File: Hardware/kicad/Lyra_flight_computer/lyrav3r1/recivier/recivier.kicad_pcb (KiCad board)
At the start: 2 copper layers, 74 parts, among them J1 USB_B_Micro, J2 Conn_01x02, J3 Conn_01x02, Q1 AO3401A, SW1 K2-1102DP-L3SW-04, SW2 K2-1102DP-L3SW-04, SW3 K2-1102DP-L3SW-04, SW4 K2-1102DP-L3SW-04, SW5 K2-1102DP-L3SW-04, U1 E22-900MM22S, U2 W25Q128JVS, U3 RP2040, U4 TXB0104RGY, U5 PCM5102A, U6 ATGM336H-5N31, U7 LIS3MDLTR, U8 RT9013-33GB_C19268157, U9 AMS1117-5.0, X1 SX1M12.000M10F30TNN

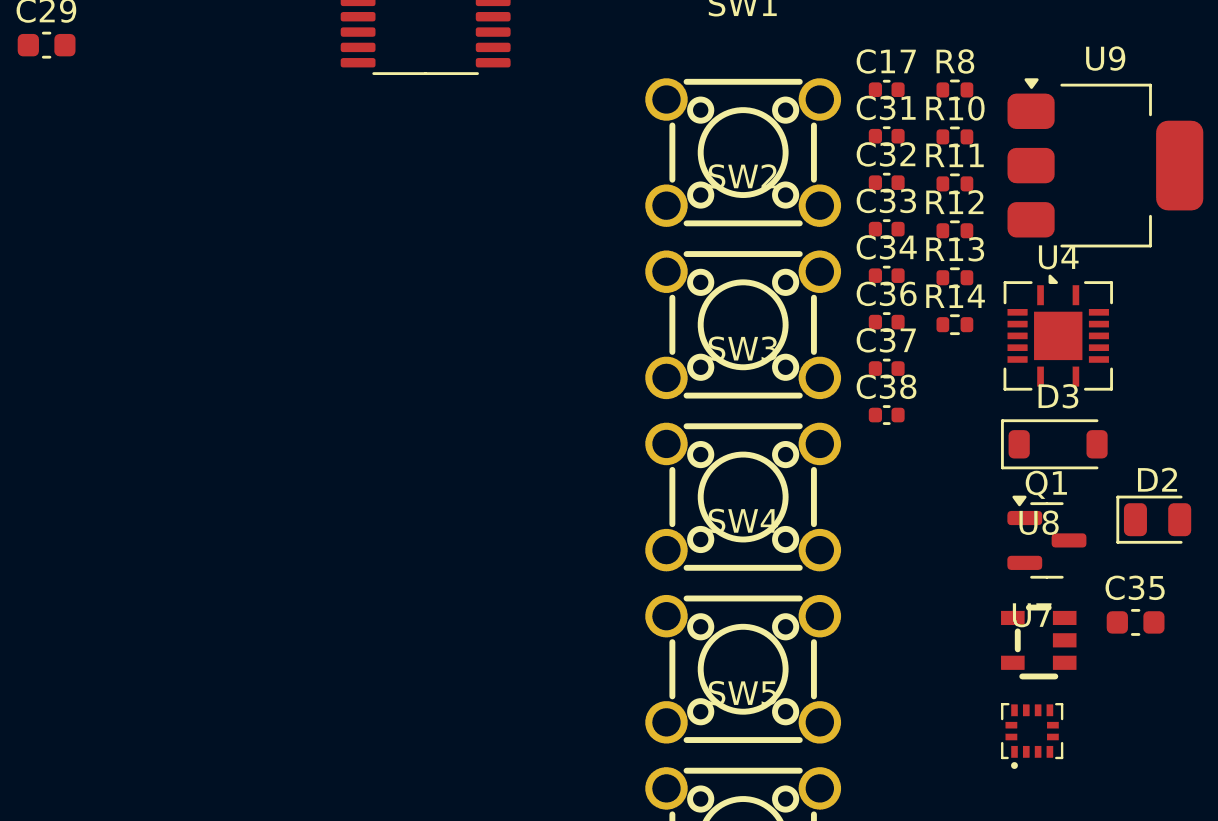
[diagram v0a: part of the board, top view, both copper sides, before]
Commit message: added batt protection for lyra, added more parts for reciver
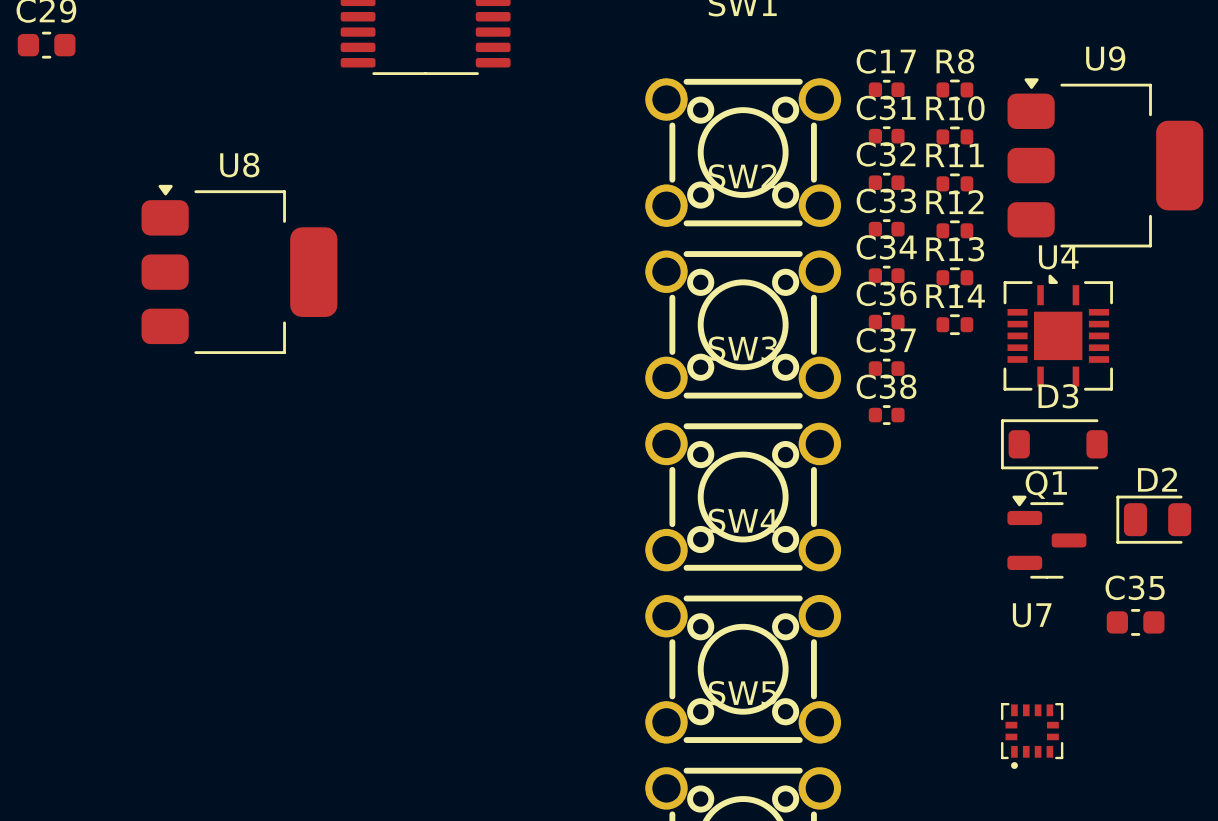
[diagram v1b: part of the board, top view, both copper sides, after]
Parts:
- U8: value RT9013-33GB_C19268157 -> AMS1117-3.3; footprint .pretty:SOT-23-5_L2.9-W1.6-P0.95-LS2.8-BR -> Package_TO_SOT_SMD:SOT-223-3_TabPin2
- moved U8 37.3 mm to (142.2, 107.9)
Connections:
- R10 pad 1: Net-(R10-Pad1) -> /BUTTON5
- R10 pad 2: /BUTTON3 -> GND
- R11 pad 1: Net-(R11-Pad1) -> /BUTTON2
- R11 pad 2: /BUTTON4 -> GND
- R12 pad 1: Net-(R10-Pad1) -> /BUTTON3
- R12 pad 2: /BUTTON1 -> GND
- R13 pad 1: Net-(R10-Pad1) -> /BUTTON1
- R13 pad 2: /BUTTON5 -> GND
- R8 pad 1: +3.3VA -> /BUTTON4
- R8 pad 2: /BUTTON2 -> GND
- SW1 pad 1: Net-(R10-Pad1) -> Net-(SW1-Pad1)
- SW1 pad 2: Net-(R11-Pad1) -> Net-(SW1-Pad2)
- SW2 pad 2: Net-(R10-Pad1) -> Net-(SW1-Pad1)
- SW3 pad 1: Net-(R10-Pad1) -> Net-(SW1-Pad1)
- SW3 pad 2: Net-(R11-Pad1) -> Net-(SW1-Pad2)
- SW4 pad 1: Net-(R11-Pad1) -> Net-(SW1-Pad2)
- SW4 pad 2: Net-(R11-Pad1) -> Net-(SW1-Pad2)
- SW5 pad 1: Net-(R10-Pad1) -> Net-(SW1-Pad1)
- SW5 pad 2: Net-(R11-Pad1) -> Net-(SW1-Pad2)
- U3 pad 30: unconnected-(U3-GPIO19-Pad30) -> /BUTTON1
- U3 pad 31: unconnected-(U3-GPIO20-Pad31) -> /BUTTON2
- U3 pad 32: unconnected-(U3-GPIO21-Pad32) -> /BUTTON3
- U3 pad 34: unconnected-(U3-GPIO22-Pad34) -> /BUTTON4
- U3 pad 35: unconnected-(U3-GPIO23-Pad35) -> /BUTTON5
- U8 pad 1: +BATT -> GND
- U8 pad 2: GND -> +3.3VA

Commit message: reciver work and finalized lyrav3r1
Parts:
- added C20: 2u2, Capacitor_SMD:C_0603_1608Metric, F.Cu at (195.6, 120.3)
- added C21: 2u2, Capacitor_SMD:C_0603_1608Metric, F.Cu at (200.9, 116.2)
- added C30: 2u2, Capacitor_SMD:C_0603_1608Metric, F.Cu at (204.6, 112.4)
- added D1: LED, LED_SMD:LED_0805_2012Metric, F.Cu at (199.1, 53.3)
- added J4: Screw_Terminal_01x02, TerminalBlock:TerminalBlock_bornier-2_P5.08mm, F.Cu at (204.2, 108.9)
- added J5: Screw_Terminal_01x02, TerminalBlock:TerminalBlock_bornier-2_P5.08mm, F.Cu at (143.2, 112.4)
- added R16: 1k, Resistor_SMD:R_0402_1005Metric, F.Cu at (154.5, 122.5)
- added R17: 40k, Resistor_SMD:R_0402_1005Metric, F.Cu at (153.5, 122.5)
- added R7: 1k, Resistor_SMD:R_0402_1005Metric, F.Cu at (201.8, 53.4)
- added R9: 470, Resistor_SMD:R_0402_1005Metric, F.Cu at (203.8, 114.1)
- added RV1: R_Potentiometer, .pretty:RES-ADJ-SMD_3314J, F.Cu at (186.9, 102.1)
- added SW6: SW_SPDT, .pretty:SW-TH_SK12D07VG4, F.Cu at (141.6, 104.5)
- DS1: footprint Display:AG12864E -> .pretty:ST7920 AZ
- J2, TP1: moved to B.Cu
- moved DS1 106.9 mm to (141.6, 97.1), turned to 90 degrees
- moved H4 99.2 mm to (205.7, 124.2)
- moved H2 90.0 mm to (205.7, 50.2)
- moved AE2 84.3 mm to (197.9, 72.1)
- moved U6 75.8 mm to (201.1, 64.7)
- moved C26 70.9 mm to (199.9, 118.2), turned to 90 degrees
- moved C27 70.7 mm to (201.1, 118.4), turned to 90 degrees
- moved C25 70.0 mm to (201.1, 113.4), turned to 90 degrees
- moved C24 69.7 mm to (199.9, 113.8), turned to 90 degrees
- moved AE1 67.5 mm to (173.6, 50.0)
- moved C23 63.6 mm to (189.7, 116.2), turned to 90 degrees
- moved C28 62.7 mm to (191.2, 118.5), turned to 90 degrees
- moved C22 62.3 mm to (191.0, 116.1), turned to 90 degrees
- moved C29 59.0 mm to (189.5, 118.6), turned to 90 degrees
- moved H3 57.2 mm to (141.7, 124.2)
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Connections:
- C35 pad 1: +BATT -> Net-(Q1-S)
- Card1 pad 5: /SCK -> /SCLK
- DS1 pad 4: /LCD CS -> /LCD CS 5V
- DS1 pad 6: /SCK 2 5V -> /SCLK 2 5V
- Q1 pad 2: +BATT -> Net-(Q1-S)
- SW1 pad 1: Net-(SW1-Pad1) -> +3.3VA
- SW1 pad 2: Net-(SW1-Pad2) -> unconnected-(SW1-Pad2)
- SW1 pad 4: /BUTTON1 -> unconnected-(SW1-Pad4)
- SW2 pad 1: +3.3VA -> unconnected-(SW2-Pad1)
- SW2 pad 2: Net-(SW1-Pad1) -> +3.3VA
- SW2 pad 4: /BUTTON2 -> unconnected-(SW2-Pad4)
- SW3 pad 1: Net-(SW1-Pad1) -> +3.3VA
- SW3 pad 2: Net-(SW1-Pad2) -> unconnected-(SW3-Pad2)
- SW3 pad 4: /BUTTON3 -> unconnected-(SW3-Pad4)
- SW4 pad 1: Net-(SW1-Pad2) -> +3.3VA
- SW4 pad 2: Net-(SW1-Pad2) -> unconnected-(SW4-Pad2)
- SW4 pad 4: /BUTTON4 -> unconnected-(SW4-Pad4)
- SW5 pad 1: Net-(SW1-Pad1) -> +3.3VA
- SW5 pad 2: Net-(SW1-Pad2) -> unconnected-(SW5-Pad2)
- SW5 pad 4: /BUTTON5 -> unconnected-(SW5-Pad4)
- U1 pad 15: /SCK -> /SCLK
- U3 pad 11: /LCD CS -> /BCK
- U3 pad 12: /SD_CS -> /SCK
- U3 pad 13: unconnected-(U3-GPIO10-Pad13) -> /DIN
- U3 pad 14: unconnected-(U3-GPIO11-Pad14) -> /LRCK
- U3 pad 17: unconnected-(U3-GPIO14-Pad17) -> /LCD CS
- U3 pad 18: /LRCK -> unconnected-(U3-GPIO15-Pad18)
- U3 pad 2: /RXEN -> /BUTTON2
- U3 pad 27: /DIN -> unconnected-(U3-GPIO16-Pad27)
- U3 pad 28: /BCK -> unconnected-(U3-GPIO17-Pad28)
- U3 pad 29: /SCK -> unconnected-(U3-GPIO18-Pad29)
- U3 pad 3: /TXEN -> /BUTTON5
- U3 pad 30: /BUTTON1 -> /SX RST
- U3 pad 31: /BUTTON2 -> /BUSY
- U3 pad 32: /BUTTON3 -> /SX CS
- U3 pad 34: /BUTTON4 -> /SCLK
- U3 pad 35: /BUTTON5 -> /MOSI
- U3 pad 36: unconnected-(U3-GPIO24-Pad36) -> /MISO
- U3 pad 38: unconnected-(U3-GPIO26_ADC0-Pad38) -> /SD_CS
- U3 pad 39: unconnected-(U3-GPIO27_ADC1-Pad39) -> /TXEN
- U3 pad 4: /SX RST -> /BUTTON3
- U3 pad 40: unconnected-(U3-GPIO28_ADC2-Pad40) -> /RXEN
- U3 pad 41: unconnected-(U3-GPIO29_ADC3-Pad41) -> /BATT SENSE
- U3 pad 5: /MOSI -> /BUTTON4
- U3 pad 6: /MISO -> /BUTTON1
- U3 pad 7: /SX CS -> unconnected-(U3-GPIO5-Pad7)
- U3 pad 8: /SCK -> unconnected-(U3-GPIO6-Pad8)
- U3 pad 9: /BUSY -> unconnected-(U3-GPIO7-Pad9)
- U4 pad 11: /MOSI 2 5V -> /SCLK 2 5V
- U4 pad 12: /LCD CS -> /MOSI 2 5V
- U4 pad 13: /SCK 2 5V -> /LCD CS 5V
- U4 pad 2: /SCK -> /LCD CS
- U4 pad 3: /LCD CS -> /MOSI
- U4 pad 4: /MOSI -> /SCLK
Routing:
- net GND: track 0.00 -> 85.5 mm, vias 0 -> 54
- net /SCL: track 0.00 -> 65.8 mm
- net /MOSI: track 0.00 -> 64.9 mm, vias 0 -> 4
- net VBUS: track 0.00 -> 64.7 mm, vias 0 -> 2
- net /LRCK: track 0.00 -> 62.4 mm
- net +5V: track 0.00 -> 62.3 mm, vias 0 -> 2
- net /BATT SENSE: track 0.00 -> 61.2 mm, vias 0 -> 2
- net /SDA: track 0.00 -> 59.7 mm, vias 0 -> 2
- net /BCK: track 0.00 -> 57.8 mm
- net /DIN: track 0.00 -> 56.5 mm
- net /SCK: track 0.00 -> 55.7 mm
- net /SCLK: track 0.00 -> 55.5 mm, vias 0 -> 4
- net +3.3VA: track 0.00 -> 54.6 mm, vias 0 -> 27
- net /BUTTON3: track 0.00 -> 54.1 mm
- net /BUTTON5: track 0.00 -> 52.8 mm
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- added copper zone on In2.Cu, net +3.3VA
- added copper zone on In1.Cu, net GND
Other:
- board outline added: 70 x 80 mm
- copper layers 2 -> 4

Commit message: work, lyra mostly final
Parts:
- added D4: LED, LED_SMD:LED_0805_2012Metric, F.Cu at (177.0, 77.1)
- added R15: 1k, Resistor_SMD:R_0402_1005Metric, F.Cu at (174.2, 77.3)
- moved R12 37.0 mm to (156.1, 90.4)
- moved R8 36.7 mm to (157.3, 88.7), turned to 180 degrees
- moved R10 36.7 mm to (154.3, 93.0), turned to 180 degrees
- moved R11 27.5 mm to (152.4, 91.3)
- moved R13 26.0 mm to (160.2, 90.3)
- moved AE2 1.24 mm to (197.9, 73.4)
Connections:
- U3 pad 18: unconnected-(U3-GPIO15-Pad18) -> /LEDINDICATION
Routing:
- net /LEDINDICATION: track 0.00 -> 14.9 mm
- net /BUTTON3: track 54.1 -> 43.5 mm
- net /LRCK: track 62.4 -> 58.4 mm
- net /SCL: track 65.8 -> 68.6 mm
- net /SDA: track 59.7 -> 61.8 mm
- net /BUTTON5: track 52.8 -> 50.8 mm
- net /BUTTON2: track 43.5 -> 41.9 mm
- net /BUTTON4: track 50.7 -> 49.2 mm
- net Net-(D4-K): track 0.00 -> 1.42 mm
- net /BCK: track 57.8 -> 56.5 mm
- net /ANT: track 1.90 -> 3.13 mm
- net +3.3VA: track 54.6 -> 55.3 mm, vias 27 -> 28
- net /SCK: track 55.7 -> 55.2 mm
- net GND: track 85.5 -> 85.6 mm, vias 54 -> 55

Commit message: reciver rework
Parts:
- removed DS1: ST7920, .pretty:ST7920 AZ

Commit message: stuffs
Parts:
- removed C31, C37, C38: 1u, Capacitor_SMD:C_0402_1005Metric
- removed Card1: TF-115K, .pretty:TF-SMD_TF-115K
- removed J4: Screw_Terminal_01x02, TerminalBlock:TerminalBlock_bornier-2_P5.08mm
- removed RV1: R_Potentiometer, .pretty:RES-ADJ-SMD_3314J
- removed SW1, SW2, SW3, SW4, SW5: K2-1102DP-L3SW-04, .pretty:SW-TH_4P-L6.0-W6.0-P4.50-LS6.5
- removed U4: TXB0104RGY, Package_DFN_QFN:Texas_S-PVQFN-N14
- removed U9: AMS1117-5.0, Package_TO_SOT_SMD:SOT-223-3_TabPin2
- added C16: 100n, Capacitor_SMD:C_0402_1005Metric, F.Cu at (180.9, 124.9)
- added C18: 10u, Capacitor_SMD:C_0603_1608Metric, F.Cu at (182.2, 125.5)
- added C19: 2u2, Capacitor_SMD:C_0603_1608Metric, F.Cu at (194.3, 137.6)
- added D5: ER-TFT032A3-3, .pretty:R-TFT032IPS-3.2, F.Cu at (146.5, 122.2)
- added J6: Conn_01x08, Connector_PinSocket_2.54mm:PinSocket_1x08_P2.54mm_Vertical, F.Cu at (153.8, 145.3)
- added J8: AudioJack4, .pretty:AUDIO-SMD_PJ-320D, F.Cu at (194.1, 128.6)
- added R18: 5.1k, Resistor_SMD:R_0402_1005Metric, F.Cu at (157.4, 129.9)
- added R19: 5.1k, Resistor_SMD:R_0402_1005Metric, F.Cu at (157.4, 127.6)
- added R20: 470, Resistor_SMD:R_0402_1005Metric, F.Cu at (192.1, 137.3)
- moved R13 52.4 mm to (157.6, 142.6)
- moved R11 49.2 mm to (157.6, 140.3), turned to 0 degrees
- moved R12 47.3 mm to (157.5, 137.7)
- moved R8 46.4 mm to (157.5, 135.1), turned to 0 degrees
- moved R10 39.7 mm to (157.4, 132.6), turned to 0 degrees
- moved C17 36.7 mm to (184.2, 91.6), turned to 180 degrees
- moved D2 30.4 mm to (173.8, 107.3), turned to -90 degrees
- moved D1 27.9 mm to (186.6, 78.2)
- moved R7 27.7 mm to (189.5, 78.3)
- moved R14 26.7 mm to (173.8, 110.0), turned to -90 degrees
- moved U6 25.5 mm to (191.4, 88.3), turned to 90 degrees
- moved C30 25.2 mm to (193.4, 135.0), turned to -90 degrees
- moved C27 24.8 mm to (188.7, 139.9)
- moved C26 24.8 mm to (187.5, 139.6)
- moved C21 24.8 mm to (188.5, 137.6)
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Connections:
- net /AUDIOOUT renamed /AUDIOOUT R
- U3 pad 11: /BCK -> /SCK
- U3 pad 12: /SCK -> /DIN
- U3 pad 13: /DIN -> /LRCK
- U3 pad 14: /LRCK -> /LCD RST
- U3 pad 18: /LEDINDICATION -> /LCD D/C
- U3 pad 2: /BUTTON2 -> /BUTTON7
- U3 pad 29: unconnected-(U3-GPIO18-Pad29) -> /LEDINDICATION
- U3 pad 3: /BUTTON5 -> /BUTTON6
- U3 pad 37: unconnected-(U3-GPIO25-Pad37) -> /LCD /WR
- U3 pad 4: /BUTTON3 -> /BUTTON5
- U3 pad 6: /BUTTON1 -> /BUTTON3
- U3 pad 7: unconnected-(U3-GPIO5-Pad7) -> /BUTTON2
- U3 pad 8: unconnected-(U3-GPIO6-Pad8) -> /BUTTON1
- U3 pad 9: unconnected-(U3-GPIO7-Pad9) -> /BCK
- U5 pad 6: unconnected-(U5-OUTL-Pad6) -> Net-(U5-OUTL)
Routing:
- net /LCD /WR: track 0.00 -> 76.4 mm, vias 0 -> 3
- net /SD_CS: track 11.0 -> 85.0 mm, vias 0 -> 2
- net /BUTTON6: track 0.00 -> 66.4 mm
- net /MISO: track 27.7 -> 92.2 mm
- net +5V: track 62.3 -> 0.00 mm, vias 2 -> 0
- net /BUTTON7: track 0.00 -> 61.9 mm
- net /LCD D/C: track 0.00 -> 51.6 mm, vias 0 -> 3
- net /LCD RST: track 0.00 -> 48.8 mm, vias 0 -> 1
- net /BUTTON1: track 35.6 -> 78.2 mm
- net /MOSI: track 64.9 -> 104.6 mm, vias 4 -> 2
- net /BUTTON2: track 41.9 -> 77.7 mm
- net /SCLK: track 55.5 -> 89.0 mm
- net +BATT: track 46.1 -> 15.8 mm
- net /BUTTON3: track 43.5 -> 73.2 mm
- net /SCL: track 68.6 -> 45.0 mm, vias 0 -> 2
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- added copper zone on B.Cu, net +3.3VA
- added copper zone on F.Cu, net GND
- removed copper zone on In2.Cu, net +3.3VA
- removed copper zone on In1.Cu, net GND
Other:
- board size 70 x 80 mm -> 66.5 x 100.3 mm
- copper layers 4 -> 2

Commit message: post order omcmit
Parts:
- removed J5: Screw_Terminal_01x02, TerminalBlock:TerminalBlock_bornier-2_P5.08mm
- removed J6: Conn_01x08, Connector_PinSocket_2.54mm:PinSocket_1x08_P2.54mm_Vertical
- removed R18, R19: 5.1k, Resistor_SMD:R_0402_1005Metric
- added BT1: Battery, SamacSys_Parts:12BH349GR, B.Cu at (142.6, 108.5)
- added G***: LOGO, LOGO, F.Cu at (150.7, 54.6)
- added J10: Conn_01x05, Connector_PinHeader_2.54mm:PinHeader_1x05_P2.54mm_Horizontal, F.Cu at (193.7, 56.5)
- added J4: Conn_01x04, Connector_PinHeader_2.54mm:PinHeader_1x04_P2.54mm_Horizontal, F.Cu at (193.7, 96.7)
- added J7: Conn_01x04, Connector_PinHeader_2.54mm:PinHeader_1x04_P2.54mm_Horizontal, F.Cu at (193.9, 71.6)
- added SW1: K2-1102DP-L3SW-04, .pretty:SW-TH_4P-L6.0-W6.0-P4.50-LS6.5, F.Cu at (170.5, 128.9)
- added SW2: K2-1102DP-L3SW-04, .pretty:SW-TH_4P-L6.0-W6.0-P4.50-LS6.5, F.Cu at (162.5, 136.4)
- added SW3: K2-1102DP-L3SW-04, .pretty:SW-TH_4P-L6.0-W6.0-P4.50-LS6.5, F.Cu at (170.5, 136.4)
- added SW4: K2-1102DP-L3SW-04, .pretty:SW-TH_4P-L6.0-W6.0-P4.50-LS6.5, F.Cu at (178.0, 136.4)
- added SW5: K2-1102DP-L3SW-04, .pretty:SW-TH_4P-L6.0-W6.0-P4.50-LS6.5, F.Cu at (170.5, 143.9)
- R16: value 1k -> 15k
- moved D2 31.1 mm to (143.3, 101.2)
- moved R14 31.1 mm to (143.3, 103.9)
- moved J2 24.8 mm to (157.4, 50.3)
- moved R8 21.5 mm to (177.7, 142.4), turned to -90 degrees
- moved TP1 20.3 mm to (160.5, 50.3)
- moved C29 19.8 mm to (196.7, 142.3)
- moved R13 18.7 mm to (164.8, 125.3), turned to -90 degrees
- moved R10 14.1 mm to (163.4, 145.4), turned to 90 degrees
- moved R12 11.8 mm to (164.1, 127.9), turned to 180 degrees
- moved R11 11.0 mm to (162.8, 130.6)
- moved C28 6.84 mm to (185.2, 142.1)
- moved C27 6.84 mm to (195.1, 142.3)
- moved C20 6.84 mm to (189.6, 143.8)
- moved C21 6.84 mm to (195.0, 140.0)
- moved C22 6.84 mm to (185.0, 139.6)
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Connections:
- U3 pad 2: /BUTTON7 -> unconnected-(U3-GPIO0-Pad2)
- U3 pad 27: unconnected-(U3-GPIO16-Pad27) -> /UART0 TX
- U3 pad 28: unconnected-(U3-GPIO17-Pad28) -> /UART0 RX
- U3 pad 3: /BUTTON6 -> unconnected-(U3-GPIO1-Pad3)
- U3 pad 5: /BUTTON4 -> /BUTTON2
- U3 pad 7: /BUTTON2 -> /BUTTON1
- U3 pad 8: /BUTTON1 -> /BUTTON4
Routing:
- net /SWD: track 9.25 -> 103.7 mm, vias 1 -> 3
- net /SWCLK: track 9.17 -> 95.1 mm, vias 1 -> 3
- net /BUTTON6: track 66.4 -> 0.00 mm
- net /BUTTON7: track 61.9 -> 0.00 mm
- net /RUN: track 5.87 -> 60.4 mm
- net /UART0 RX: track 0.00 -> 44.2 mm, vias 0 -> 2
- net /UART0 TX: track 0.00 -> 44.0 mm, vias 0 -> 2
- net (no net): track 0.00 -> 34.9 mm
- net /MISO: track 92.2 -> 115.6 mm, vias 2 -> 5
- net /SCLK: track 89.0 -> 110.5 mm, vias 4 -> 6
- net /BUTTON1: track 78.2 -> 58.2 mm, vias 0 -> 2
- net /AUDIOOUT L: track 23.3 -> 3.59 mm, vias 1 -> 0
- net /SCL: track 45.0 -> 62.5 mm, vias 2 -> 3
- net /SDA: track 48.6 -> 63.7 mm
- net /MOSI: track 104.6 -> 119.4 mm, vias 2 -> 3
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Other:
- board size 66.5 x 100.3 mm -> 66 x 100 mm
- board text added: "+ RX TX _"
- board text added: "+ SCLK MISO MOSI -"
- board text added: "+ SDA SCL -"
- board text added: "LYRA-GS1"
- board text added: "POLARIS ROCKETRY SYSTEMS"
